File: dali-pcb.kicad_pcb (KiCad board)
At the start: 2 copper layers, 180.4 x 113 mm, 60 parts, among them J1 12-22.5V DC, J10 5V DC, J11 5V DC, J12 5V DC, J13 5V DC, J14 5V DC, J15 GND, J2 DALI BUS, J20 LOLIN-S3 (L), J21 LOLIN-S3 (R), J22 ESP32-S3-DEVKITC-1 (L), J23 ESP32-S3-DEVKITC-1 (R), J24 LOLIN-S3-MINI (L), J25 LOLIN-S3-MINI (R), J26 LOLIN-S2-MINI (L), J27 LOLIN-S2-MINI (R), J3 DALI BUS, J30 FTDI-MCU, J31 UART-DALI, J4 DALI BUS, J40 A10, J41 A5-1, J42 A5-2, J43 A2-1, J44 A2-2, J45 A2-3, J46 A2-4, J47 A2-5, J50 D8, J51 D4-1, J52 D4-2, J53 D2-1, J54 D2-2, J55 D2-3, J56 D2-4, J60 D1-11, J61 D1-12, J62 D1-13, J63 D1-14, Q1 PZT2222A, Q2 MMBT2222A, U1 TCLT1000, U2 TCLT1000

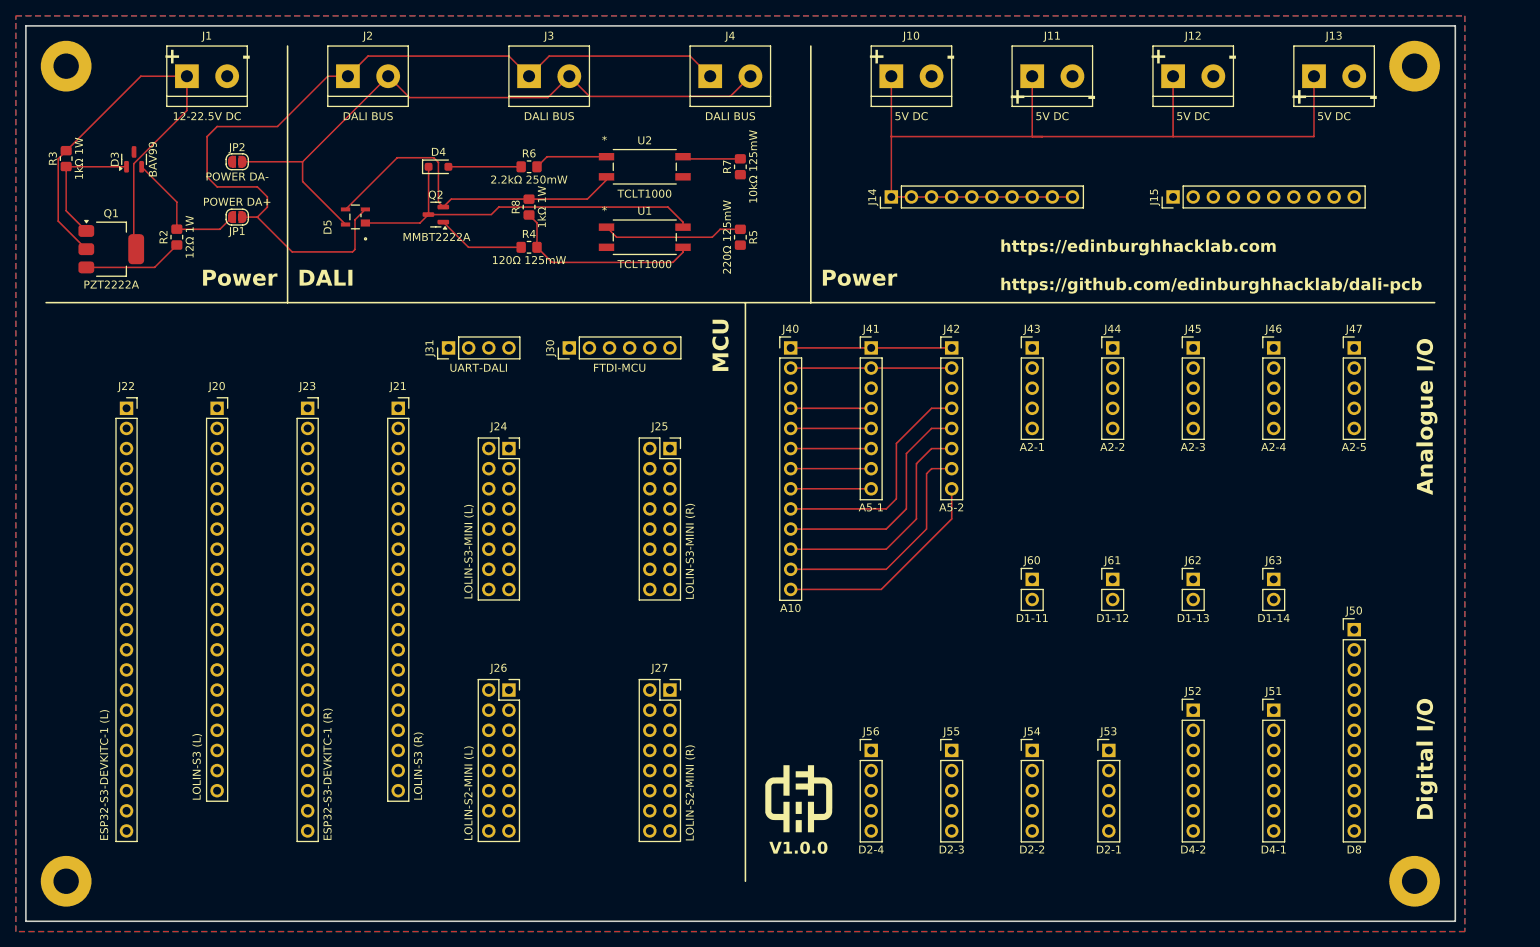
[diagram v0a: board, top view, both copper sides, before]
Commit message: Don't connect unused GPIOs together across MCUs
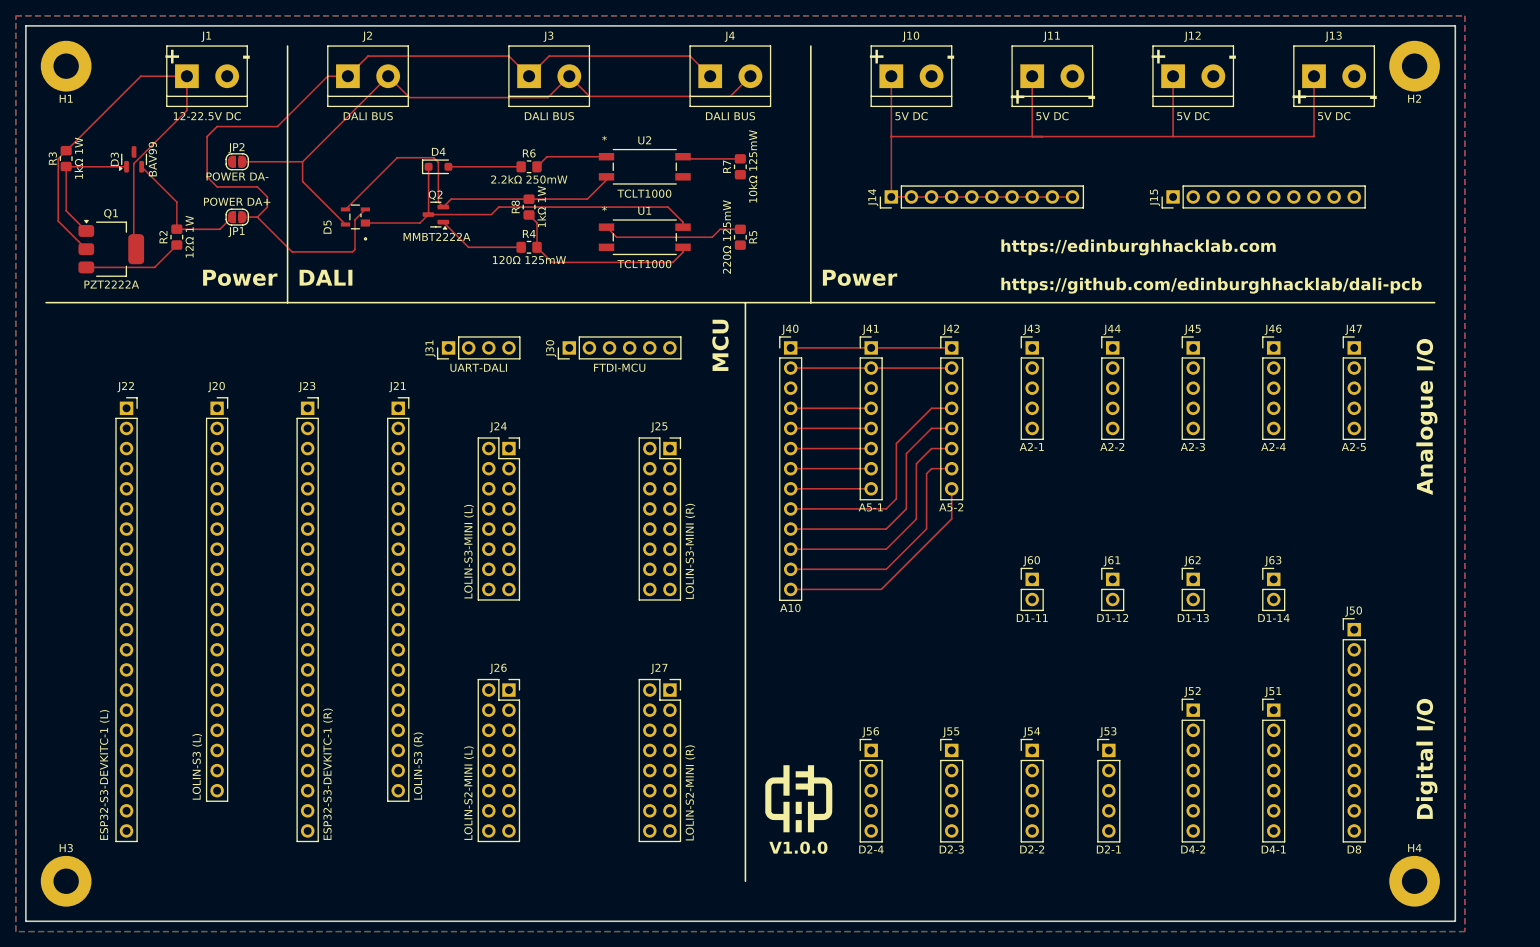
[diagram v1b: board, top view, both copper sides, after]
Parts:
- turned H1 to 180 degrees
- turned H2 to 180 degrees
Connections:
- J20 pad 8: /Microcontroller/ESP32_GPIO15 -> unconnected-(J20-Pin_8-Pad8)
- J21 pad 12: /Microcontroller/ESP32_GPIO45 -> unconnected-(J21-Pin_12-Pad12)
- J21 pad 13: /Microcontroller/ESP32_GPIO48 -> unconnected-(J21-Pin_13-Pad13)
- J21 pad 14: /Microcontroller/ESP32_GPIO47 -> unconnected-(J21-Pin_14-Pad14)
- J21 pad 6: /Microcontroller/ESP32_GPIO42 -> unconnected-(J21-Pin_6-Pad6)
- J21 pad 7: /Microcontroller/ESP32_GPIO41 -> unconnected-(J21-Pin_7-Pad7)
- J22 pad 8: /Microcontroller/ESP32_GPIO15 -> unconnected-(J22-Pin_8-Pad8)
- J23 pad 14: /Microcontroller/ESP32_GPIO45 -> unconnected-(J23-Pin_14-Pad14)
- J23 pad 15: /Microcontroller/ESP32_GPIO48 -> unconnected-(J23-Pin_15-Pad15)
- J23 pad 16: /Microcontroller/ESP32_GPIO47 -> unconnected-(J23-Pin_16-Pad16)
- J23 pad 6: /Microcontroller/ESP32_GPIO42 -> unconnected-(J23-Pin_6-Pad6)
- J23 pad 7: /Microcontroller/ESP32_GPIO41 -> unconnected-(J23-Pin_7-Pad7)
- J25 pad 16: /Microcontroller/ESP32_GPIO15 -> unconnected-(J25-Pin_16-Pad16)
- J25 pad 2: /Microcontroller/ESP32_GPIO33 -> unconnected-(J25-Pin_2-Pad2)
- J25 pad 4: /Microcontroller/ESP32_GPIO37 -> unconnected-(J25-Pin_4-Pad4)
- J25 pad 5: /Microcontroller/ESP32_GPIO36 -> unconnected-(J25-Pin_5-Pad5)
- J25 pad 6: /Microcontroller/ESP32_GPIO38 -> unconnected-(J25-Pin_6-Pad6)
- J25 pad 7: /Microcontroller/ESP32_GPIO35 -> unconnected-(J25-Pin_7-Pad7)
- J25 pad 8: /Microcontroller/ESP32_GPIO34 -> unconnected-(J25-Pin_8-Pad8)
- J27 pad 3: /Microcontroller/ESP32_GPIO37 -> unconnected-(J27-Pin_3-Pad3)
- J27 pad 4: /Microcontroller/ESP32_GPIO38 -> unconnected-(J27-Pin_4-Pad4)
- J27 pad 5: /Microcontroller/ESP32_GPIO35 -> unconnected-(J27-Pin_5-Pad5)
- J27 pad 6: /Microcontroller/ESP32_GPIO36 -> unconnected-(J27-Pin_6-Pad6)
- J27 pad 7: /Microcontroller/ESP32_GPIO33 -> unconnected-(J27-Pin_7-Pad7)
- J27 pad 8: /Microcontroller/ESP32_GPIO34 -> unconnected-(J27-Pin_8-Pad8)

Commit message: Label all the I/O pins
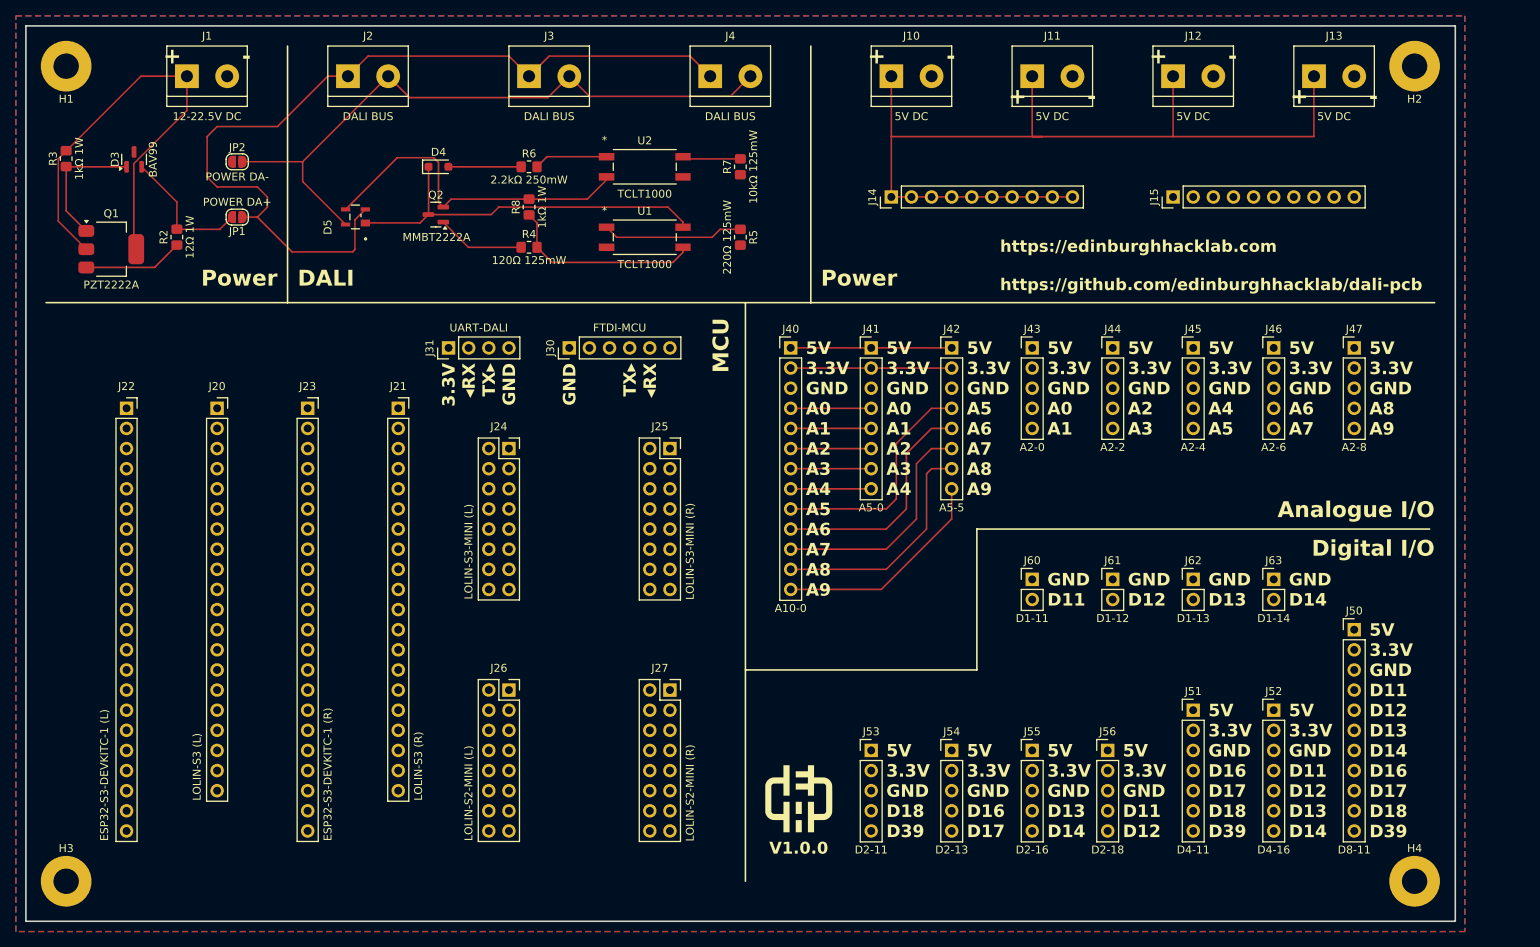
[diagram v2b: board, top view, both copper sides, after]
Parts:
- J40: value A10 -> A10-0
- J41: value A5-1 -> A5-0
- J42: value A5-2 -> A5-5
- J43: value A2-1 -> A2-0
- J45: value A2-3 -> A2-4
- J46: value A2-4 -> A2-6
- J47: value A2-5 -> A2-8
- J50: value D8 -> D8-11
- J51: value D4-1 -> D4-11
- J52: value D4-2 -> D4-16
- J53: value D2-1 -> D2-11
- J54: value D2-2 -> D2-13
- J55: value D2-3 -> D2-16
- J56: value D2-4 -> D2-18
- moved J53 30.0 mm to (121.9, 106.7)
- moved J56 29.8 mm to (151.8, 106.7)
- moved J51 10.2 mm to (162.6, 101.6)
- moved J52 10.2 mm to (172.7, 101.6)
- moved J54 10.2 mm to (132.1, 106.7)
- moved J55 10.2 mm to (142.2, 106.7)
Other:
- board text added: "3.3V ◂RX TX▸ GND"
- board text added: "5V 3.3V GND A0 A1"
- board text added: "5V 3.3V GND A0 A1 A2 A3 A4"
- board text added: "5V 3.3V GND A0 A1 A2 A3 A4 A5 A6 A7 A8 A9"
- board text added: "5V 3.3V GND A2 A3"
- board text added: "5V 3.3V GND A4 A5"
- board text added: "5V 3.3V GND A5 A6 A7 A8 A9"
- board text added: "5V 3.3V GND A6 A7"
- board text added: "5V 3.3V GND A8 A9"
- board text added: "5V 3.3V GND D11 D12"
- board text added: "5V 3.3V GND D11 D12 D13 D14"
- board text added: "5V 3.3V GND D11 D12 D13 D14 D16 D17 D18 D39"
- board text added: "5V 3.3V GND D13 D14"
- board text added: "5V 3.3V GND D16 D17"
- board text added: "5V 3.3V GND D16 D17 D18 D39"
- board text added: "5V 3.3V GND D18 D39"
- board text added: "GND D11"
- board text added: "GND D12"
- board text added: "GND D13"
- board text added: "GND D14"
- board text added: "GND TX▸ ◂RX"

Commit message: Fix screw terminal orientation and mounting holes
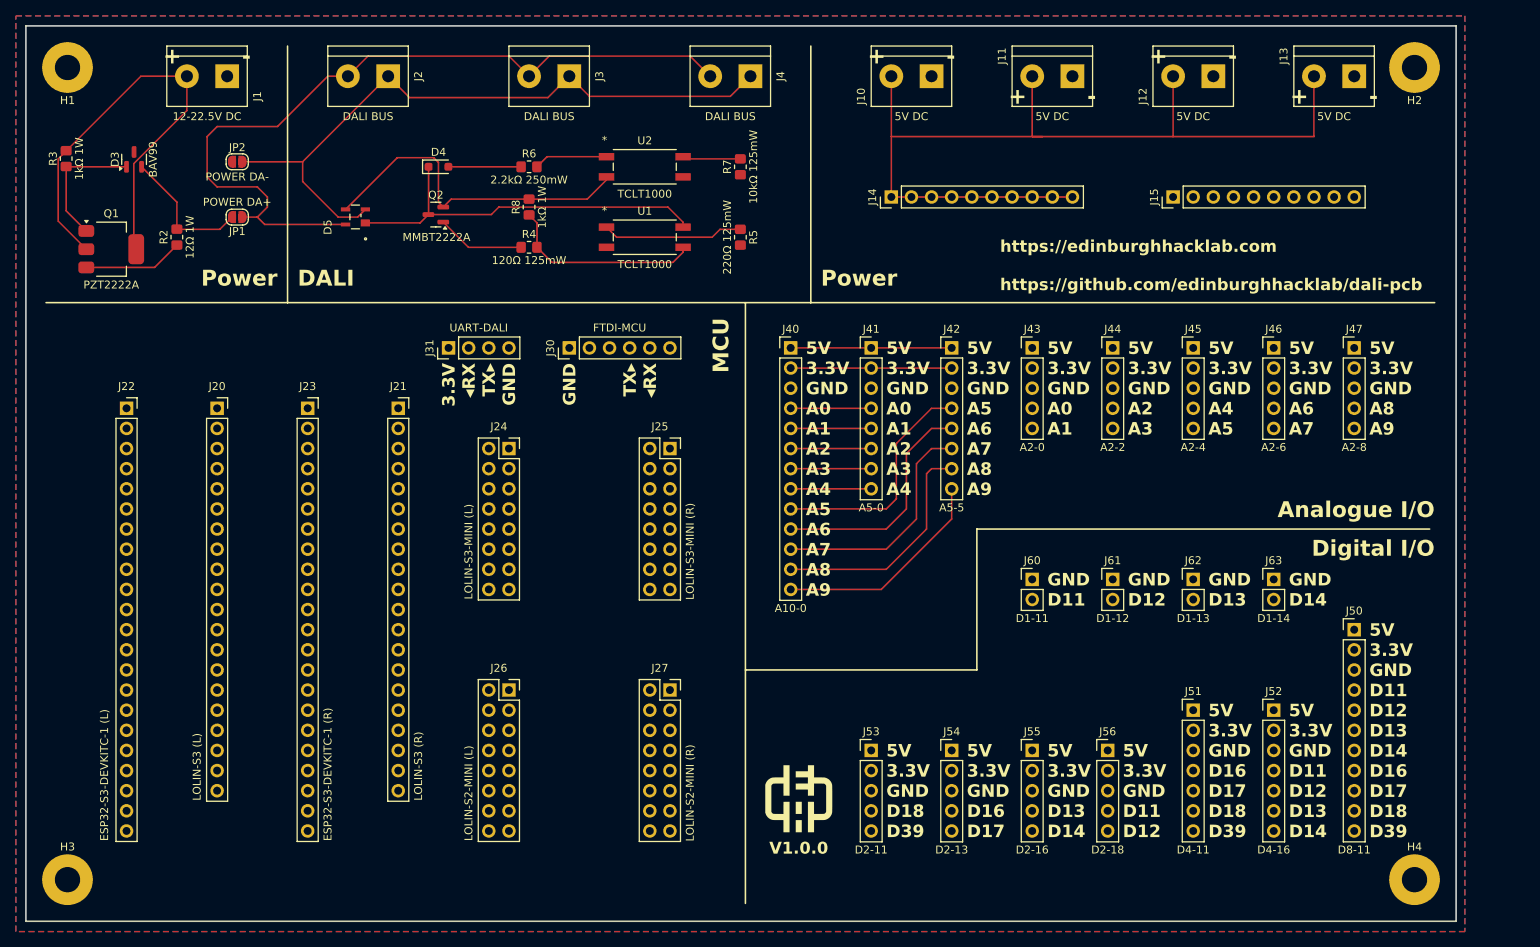
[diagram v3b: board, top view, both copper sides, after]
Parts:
- moved J4 5.08 mm to (106.7, 21.6), turned to 180 degrees
- moved J1 5.08 mm to (40.6, 21.6), turned to 180 degrees
- moved J10 5.08 mm to (129.5, 21.6), turned to 180 degrees
- moved J2 5.08 mm to (61.0, 21.6), turned to 180 degrees
- moved J3 5.08 mm to (83.8, 21.6), turned to 180 degrees
- moved J11 5.08 mm to (147.3, 21.6), turned to 180 degrees
- moved J12 5.08 mm to (165.1, 21.6), turned to 180 degrees
- moved J13 5.08 mm to (182.9, 21.6), turned to 180 degrees
- moved H3 0.26 mm to (20.5, 123.0)
- moved H1 0.24 mm to (20.5, 20.5)
- moved H4 0.20 mm to (190.5, 123.0)
- moved H2 0.17 mm to (190.5, 20.5)
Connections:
- D5 pad 2: /DALI/DA+ -> /DALI/DA-
- D5 pad 4: /DALI/DA- -> /DALI/DA+
- J1 pad 1: +12-22.5V DC -> GND
- J1 pad 2: GND -> +12-22.5V DC
- J10 pad 1: +5V -> GND
- J10 pad 2: GND -> +5V
- J11 pad 1: +5V -> GND
- J11 pad 2: GND -> +5V
- J12 pad 1: +5V -> GND
- J12 pad 2: GND -> +5V
- J13 pad 1: +5V -> GND
- J13 pad 2: GND -> +5V
- J2 pad 1: /DALI/DA+ -> /DALI/DA-
- J2 pad 2: /DALI/DA- -> /DALI/DA+
- J3 pad 1: /DALI/DA+ -> /DALI/DA-
- J3 pad 2: /DALI/DA- -> /DALI/DA+
- J4 pad 1: /DALI/DA+ -> /DALI/DA-
- J4 pad 2: /DALI/DA- -> /DALI/DA+
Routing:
- net /DALI/DA+: track 109.4 -> 101.1 mm
- net /DALI/DA-: track 83.1 -> 85.6 mm
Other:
- board size 180.4 x 113 mm -> 180.5 x 113 mm

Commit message: Add easy MCU traces and all the analogue I/O internal traces
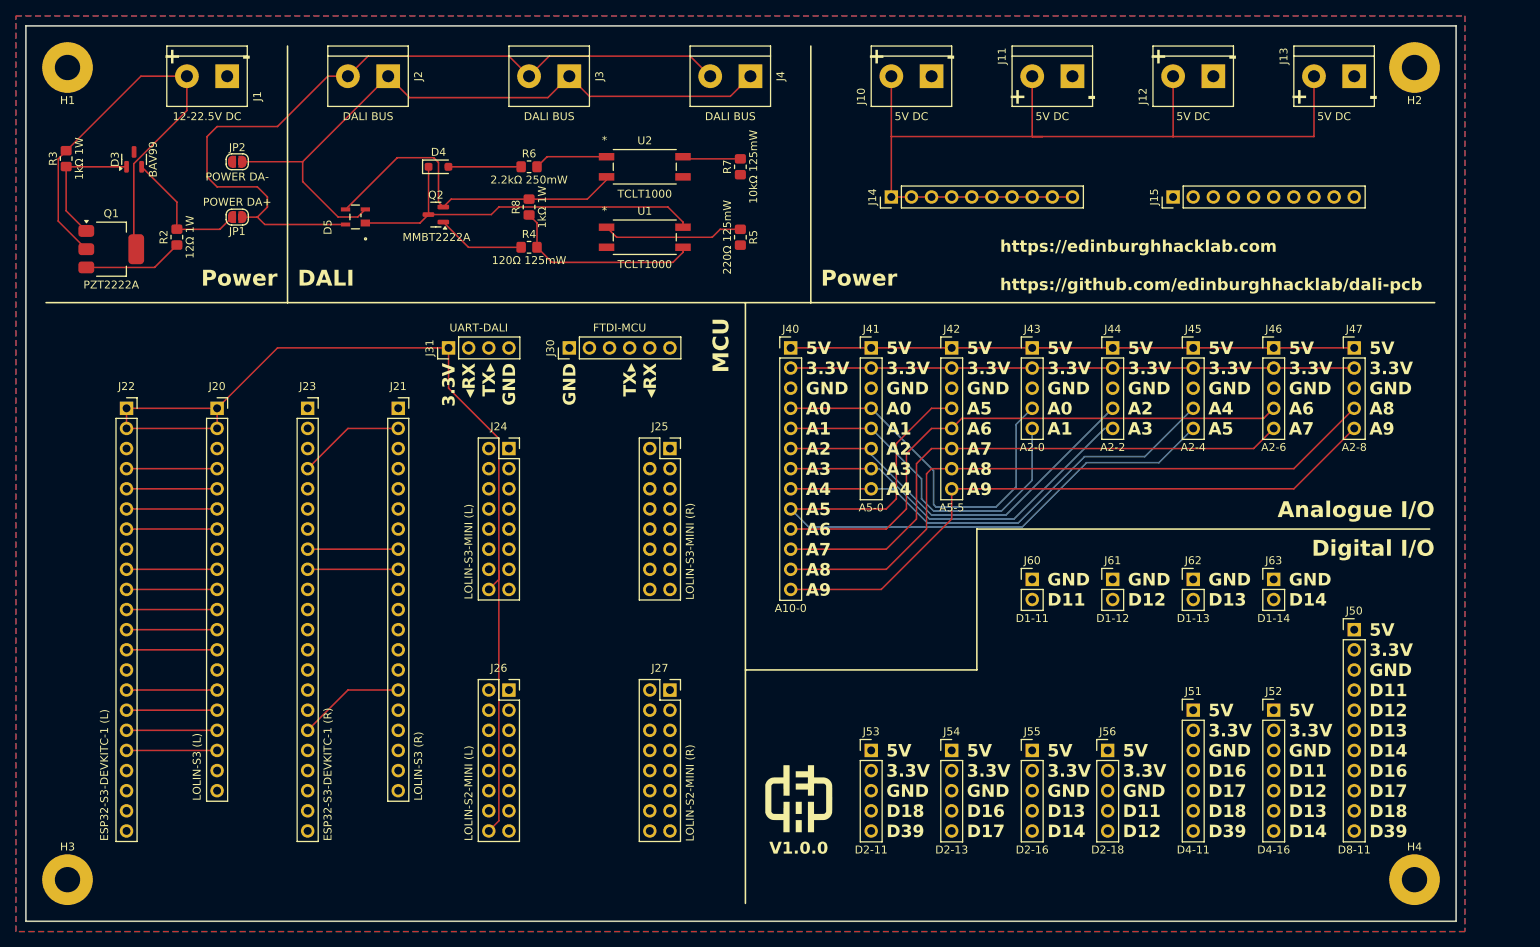
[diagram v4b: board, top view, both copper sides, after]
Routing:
- net +3.3V: track 20.3 -> 198.4 mm
- net /IO/IO_A5: track 29.7 -> 98.0 mm
- net /IO/IO_A9: track 27.8 -> 93.2 mm
- net /IO/IO_A8: track 29.7 -> 95.1 mm
- net /IO/IO_A4: track 10.2 -> 70.0 mm
- net /IO/IO_A6: track 29.7 -> 82.8 mm
- net /IO/IO_A7: track 29.7 -> 82.8 mm
- net /IO/IO_A2: track 10.2 -> 61.6 mm
- net /IO/IO_A0: track 10.2 -> 61.4 mm
- net +5V: track 135.9 -> 186.7 mm
- net /IO/IO_A3: track 10.2 -> 59.4 mm
- net /IO/IO_A1: track 10.2 -> 44.4 mm
- net /DALI/DALI_TX: track 0.00 -> 13.5 mm
- net /IO/IO_D39: track 0.00 -> 11.4 mm
- net /DALI/DALI_RX: track 6.97 -> 18.4 mm
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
